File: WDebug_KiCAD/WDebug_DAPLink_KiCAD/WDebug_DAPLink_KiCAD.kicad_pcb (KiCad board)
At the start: 2 copper layers, 55 x 34 mm, 44 parts, among them J1 Conn_01x04, J2 Conn_02x04_UART_SW, J3 Conn_01x20_Female, J4 Conn_01x05_Male, J5 01x18_Female_Fan, J6 3.3V_Conn, P1 USB_C_Plug_USB2.0, SW1 SW_Rst, U1 XC6228D332VR-G-matrix_display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, U2 STM32F103C8Tx, Y1 8MHz

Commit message: 修正DAPlink 1.5版本 串口信号修改，新加一路串口
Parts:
- moved J2 1.31 mm to (133.8, 89.9)
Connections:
- J2 pad 2: /T_RX -> /MCU_RX2
- J2 pad 4: /T_TX -> /MCU_TX2
- J2 pad 6: /T_RX -> /MCU_RX1
- J2 pad 8: /T_TX -> /MCU_TX1
- U2 pad 12: /T_TX -> /MCU_TX2
- U2 pad 13: /T_RX -> /MCU_RX2
- U2 pad 17: Net-(U2-Pad17) -> /PWR_RED
- U2 pad 29: Net-(U2-Pad29) -> /T_SWO
- U2 pad 30: /PWR_RED -> /MCU_TX1
- U2 pad 31: /T_SWO -> /MCU_RX1
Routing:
- net /T_TX: track 31.5 -> 0.00 mm, vias 1 -> 0
- net /T_RX: track 27.5 -> 0.00 mm, vias 1 -> 0
- net /MCU_TX2: track 0.00 -> 27.3 mm, vias 0 -> 1
- net /MCU_TX1: track 0.00 -> 24.2 mm
- net /MCU_RX2: track 0.00 -> 22.3 mm, vias 0 -> 1
- net /MCU_RX1: track 0.00 -> 19.5 mm
- net /PWR_RED: track 16.8 -> 31.8 mm, vias 2 -> 3
- net GND: track 59.3 -> 69.3 mm, vias 28 -> 29
- net /T_SWO: track 35.1 -> 32.5 mm
- net /TX1: track 30.4 -> 32.4 mm
- net /RX1: track 28.4 -> 29.8 mm
- net /TX2: track 19.4 -> 20.7 mm
- net /RX2: track 18.0 -> 19.3 mm
- net /3_3V_Conn: track 44.4 -> 45.3 mm
- net /T_SWDIO: track 55.3 -> 54.6 mm
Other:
- board text added: "PA10"
- board text added: "PA2"
- board text added: "PA3"
- board text added: "PA9"
- board text added: "TX2"
- board text added: "WDebug_DAPLink_V1.5 Chenweipeng 20200630"
- board text removed: "WDebug_DAPLink_V1.4 Chenweipeng 20200515"

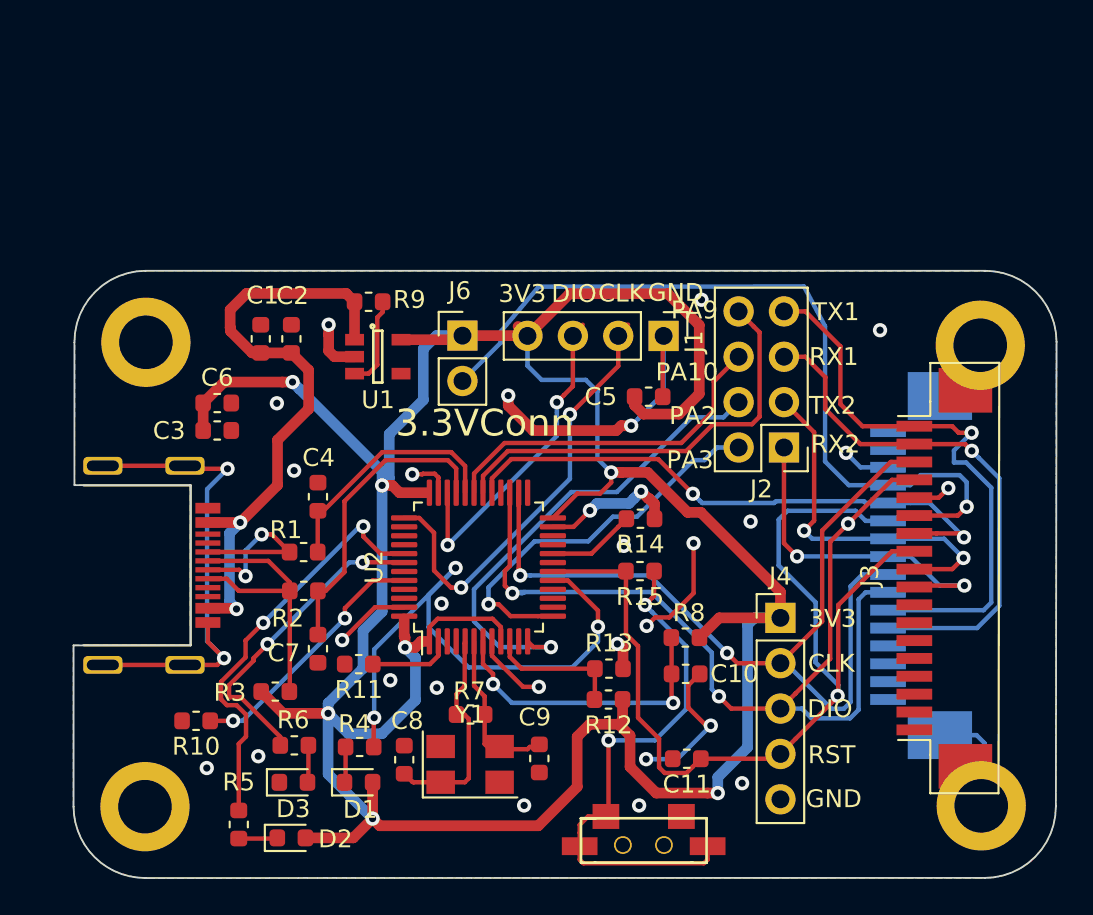
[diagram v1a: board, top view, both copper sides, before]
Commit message: 新加转接板，准备V1.7版本的修改思路和改进点
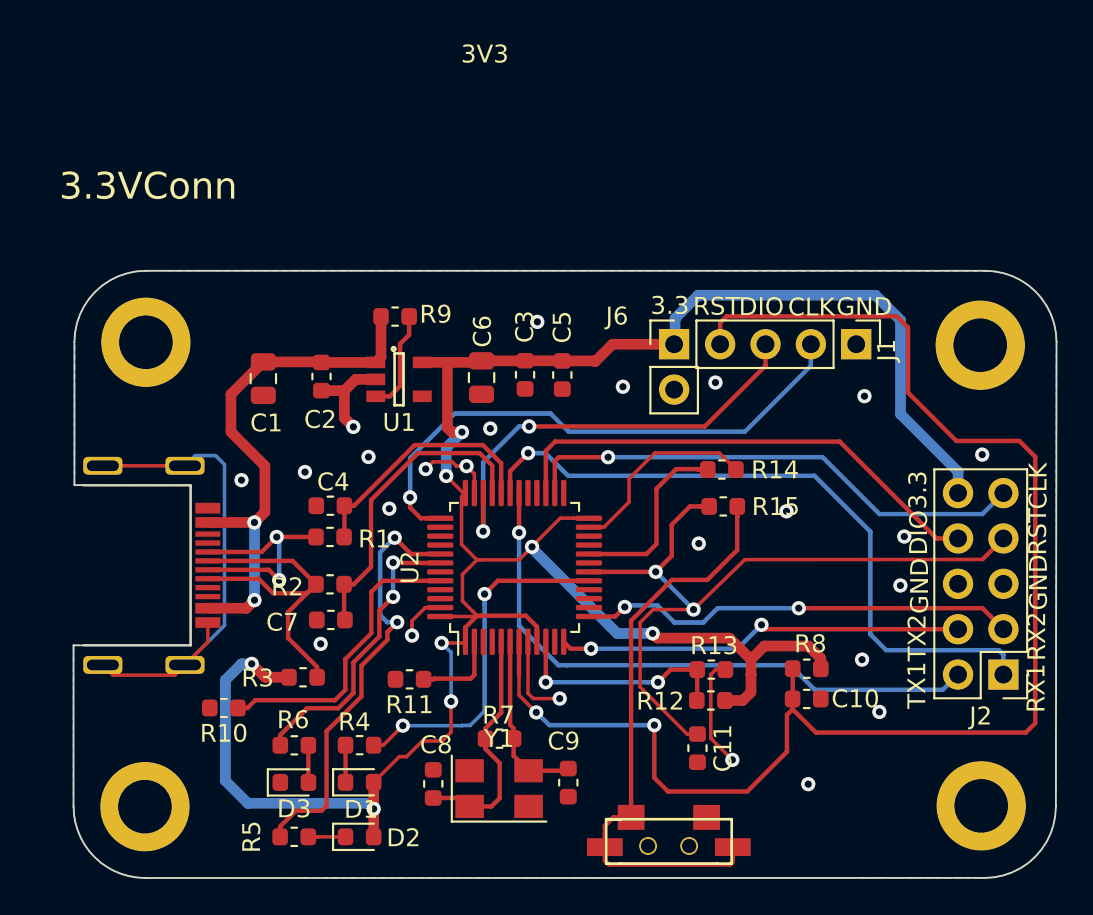
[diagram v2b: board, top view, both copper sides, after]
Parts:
- removed J3: Conn_01x20_Female, WDebug_KiCAD:1x18_P1.0mm
- removed J4: Conn_01x05_Male, Connector_PinHeader_2.54mm:PinHeader_1x05_P2.54mm_Vertical
- removed J5: 01x18_Female_Fan, WDebug_DAPLink:1x16_P1.0mm
- C1, C6: footprint Capacitor_SMD:C_0603_1608Metric -> Capacitor_SMD:C_0805_2012Metric
- J2: value Conn_02x04_UART_SW -> Conn_02x05_Counter_Clockwise; footprint Connector_PinHeader_2.54mm:PinHeader_2x04_P2.54mm_Vertical -> Connector_PinHeader_2.54mm:PinHeader_2x05_P2.54mm_Vertical
- moved J2 17.7 mm to (146.0, 102.6)
- moved C3 17.5 mm to (119.3, 85.8), turned to 270 degrees
- moved C6 14.9 mm to (116.8, 86.0), turned to 270 degrees
- moved J6 11.9 mm to (127.6, 84.1)
- moved J1 10.8 mm to (137.8, 84.1)
- moved R8 7.01 mm to (135.0, 102.3)
- moved C10 6.92 mm to (135.0, 104.0)
- moved R15 5.90 mm to (130.4, 93.2)
- moved R13 5.73 mm to (129.7, 102.3)
- moved R12 5.73 mm to (129.7, 104.1)
- moved R14 5.32 mm to (130.3, 91.1)
- moved C5 4.98 mm to (121.3, 85.8), turned to 270 degrees
- moved D2 3.82 mm to (110.0, 111.7)
- moved R5 3.18 mm to (106.3, 111.7), turned to 0 degrees
- moved R11 2.97 mm to (112.8, 102.9)
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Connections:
- J1 pad 4: +3V3 -> /IF_RST
- J2 pad 1: /RX2 -> /MCU_RX1
- J2 pad 2: /MCU_RX2 -> /MCU_TX1
- J2 pad 3: /TX2 -> /MCU_RX2
- J2 pad 5: /RX1 -> GND
- J2 pad 6: /MCU_RX1 -> GND
- J2 pad 7: /TX1 -> /TG_RST
- J2 pad 8: /MCU_TX1 -> /T_SWDIO
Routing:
- net /IF_RST: track 16.8 -> 81.3 mm
- net +3V3: track 180.3 -> 131.4 mm, vias 7 -> 8
- net /3_3V_Conn: track 45.3 -> 0.00 mm, vias 1 -> 0
- net /T_SWO: track 32.5 -> 0.00 mm, vias 2 -> 0
- net /TX1: track 32.4 -> 0.00 mm, vias 1 -> 0
- net GND: track 69.3 -> 37.5 mm, vias 29 -> 24
- net /RX1: track 29.8 -> 0.00 mm, vias 1 -> 0
- net /T_SWDIO: track 54.6 -> 27.9 mm, vias 3 -> 0
- net /T_SWCLK: track 50.4 -> 28.8 mm, vias 2 -> 1
- net /TX2: track 20.7 -> 0.00 mm, vias 2 -> 0
- net /RX2: track 19.3 -> 0.00 mm, vias 2 -> 0
- net /MCU_RX1: track 19.5 -> 38.4 mm, vias 0 -> 1
- net /TG_RST: track 57.1 -> 42.5 mm, vias 1 -> 2
- net /PWR_RED: track 31.8 -> 19.7 mm, vias 3 -> 2
- net /MCU_TX1: track 24.2 -> 33.8 mm, vias 0 -> 1
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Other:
- net class Default: clearance 0.2 -> 0.1; trace_width 0.25 -> 0.2
- rule trace_clearance: 0.2 -> 0.1
- board text added: "3.3"
- board text added: "WDebug_DAPLink_V1.6 Chenweipeng 20211008"
- board text removed: "PA10"
- board text removed: "PA2"
- board text removed: "PA3"
- board text removed: "PA9"
- board text removed: "WDebug_DAPLink_V1.5 Chenweipeng 20200630"

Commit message: 修改V1.7版本 typec元件切换/晶振封装切换/SWD接口切换/新加3.3v调试电阻
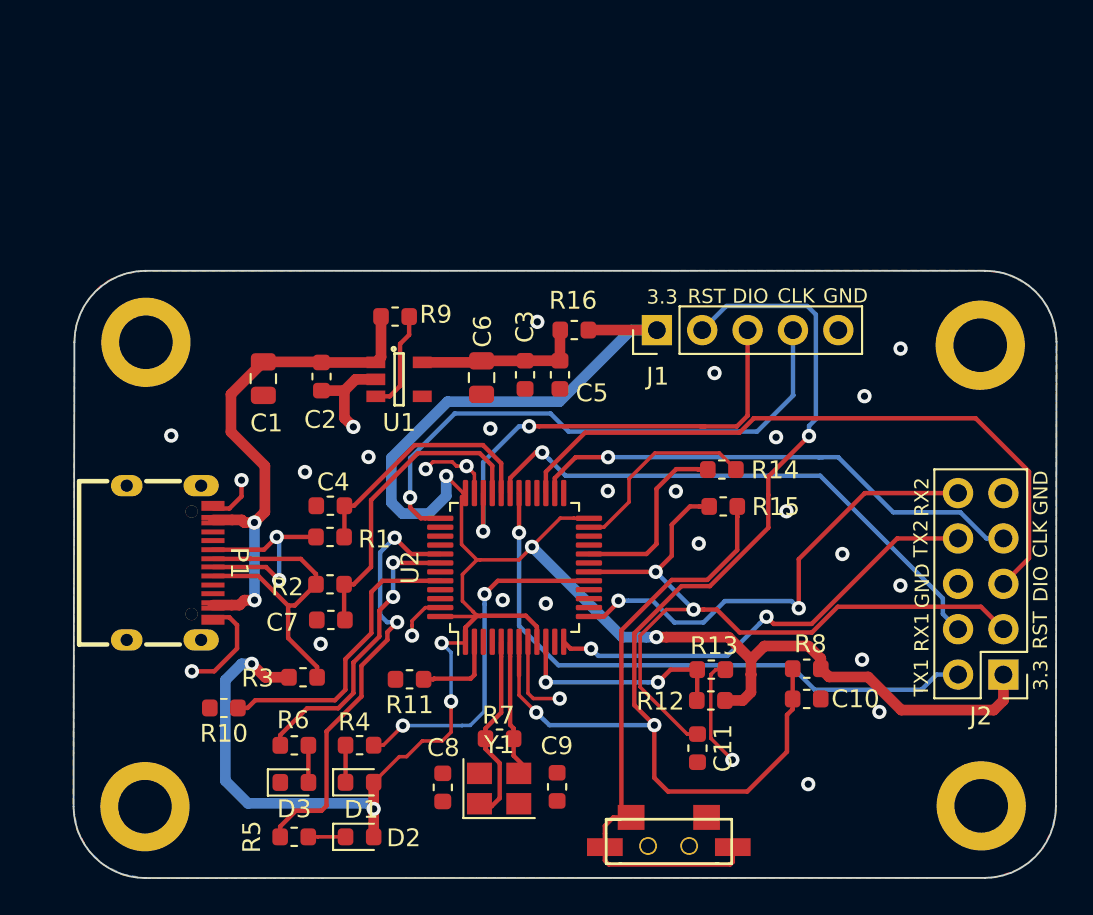
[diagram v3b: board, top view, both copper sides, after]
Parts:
- removed J6: 3.3V_Conn, Connector_PinHeader_2.54mm:PinHeader_1x02_P2.54mm_Vertical
- added R16: 0, Resistor_SMD:R_0603_1608Metric, F.Cu at (122.0, 83.3)
- J1: value Conn_01x04 -> Conn_01x05_Male; footprint Connector_PinHeader_2.54mm:PinHeader_1x04_P2.54mm_Vertical -> Connector_PinHeader_2.54mm:PinHeader_1x05_P2.54mm_Vertical
- J2: value Conn_02x05_Counter_Clockwise -> ConnDebug
- P1: value USB_C_Plug_USB2.0 -> USB_C_Plug_USB2.0-Connector; footprint WDebug_DAPLink:USB-Type-C -> library:USB-C-SMD_KH-TYPE-C-16P
- Y1: footprint Crystal:Crystal_SMD_5032-4Pin_5.0x3.2mm -> Crystal:Crystal_SMD_3225-4Pin_3.2x2.5mm
- moved J1 11.2 mm to (126.6, 83.3), turned to 90 degrees
- moved P1 2.95 mm to (99.4, 96.3)
- moved C9 0.67 mm to (121.0, 108.9)
- moved C8 0.57 mm to (114.6, 108.9)
- moved C5 0.13 mm to (121.2, 85.8)
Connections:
- C3 pad 1: +3V3 -> Net-(C3-Pad1)
- C5 pad 1: +3V3 -> Net-(C3-Pad1)
- C6 pad 1: +3V3 -> Net-(C3-Pad1)
- J1 pad 1: GND -> +3V3
- J1 pad 2: /IF_SWCLK -> /IF_RST
- J1 pad 4: /IF_RST -> /IF_SWCLK
- J2 pad 1: /MCU_RX1 -> +3V3
- J2 pad 10: +3V3 -> /MCU_RX2
- J2 pad 3: /MCU_RX2 -> /TG_RST
- J2 pad 4: /MCU_TX2 -> /MCU_RX1
- J2 pad 5: GND -> /T_SWDIO
- J2 pad 7: /TG_RST -> /T_SWCLK
- J2 pad 8: /T_SWDIO -> /MCU_TX2
- J2 pad 9: /T_SWCLK -> GND
- U1 pad 5: +3V3 -> Net-(C3-Pad1)
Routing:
- net Net-(P1-PadS1): track 27.4 -> 0.00 mm
- net /IF_RST: track 81.3 -> 63.4 mm, vias 2 -> 3
- net /T_SWDIO: track 27.9 -> 37.6 mm
- net Net-(C3-Pad1): track 0.00 -> 9.47 mm
- net GND: track 37.5 -> 46.1 mm, vias 24 -> 29
- net /MCU_RX1: track 38.4 -> 31.1 mm
- net +3V3: track 131.4 -> 124.9 mm, vias 8 -> 7
- net /MCU_TX2: track 22.9 -> 25.5 mm
- net Net-(C8-Pad1): track 13.6 -> 11.3 mm
- net Net-(C9-Pad1): track 9.92 -> 7.82 mm
- net /MCU_RX2: track 24.7 -> 26.5 mm
- net /IF_SWDIO: track 25.3 -> 26.9 mm
- net Net-(P1-PadA6): track 19.2 -> 18.3 mm
- net /IF_SWCLK: track 31.3 -> 32.1 mm
- net VBUS: track 29.5 -> 28.9 mm
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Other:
- outline, holes or cut-outs redrawn
- net class Default: trace_width 0.2 -> 0.25
- board text added: "WDebug_DAPLink_V1.7 Chenweipeng 20220112"
- board text removed: "3.3VConn"
- board text removed: "3V3"
- board text removed: "WDebug_DAPLink_V1.6 Chenweipeng 20211008"
